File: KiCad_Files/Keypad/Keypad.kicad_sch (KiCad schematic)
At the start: 0 parts

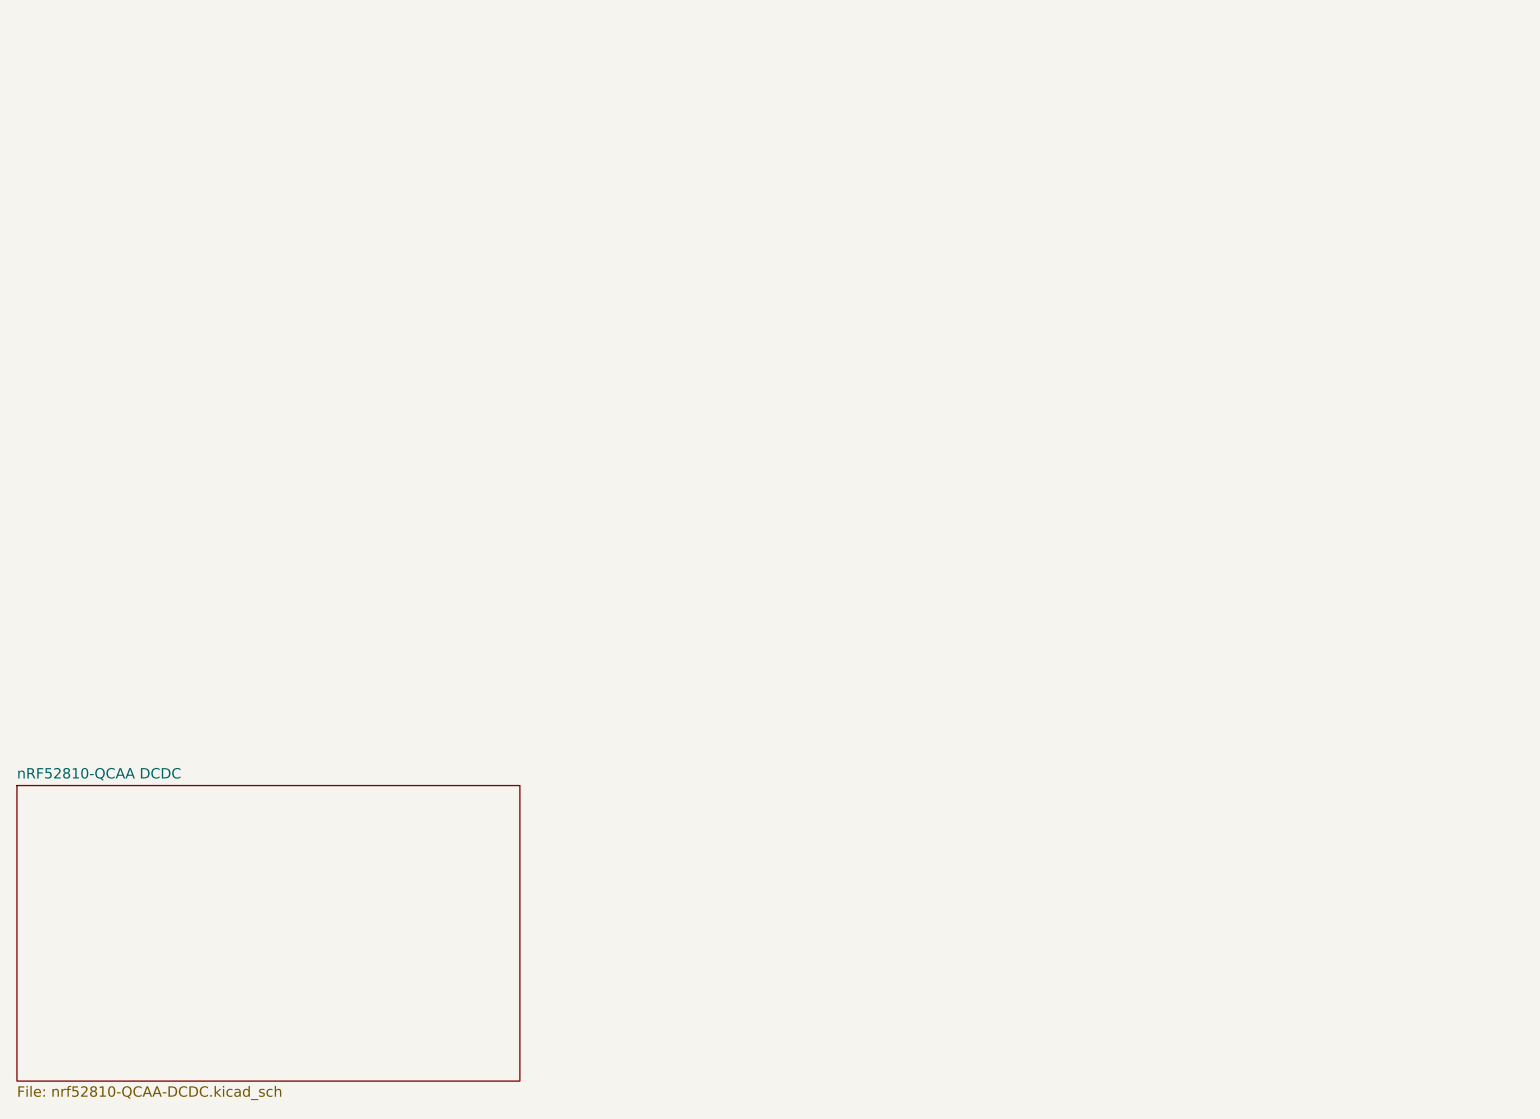
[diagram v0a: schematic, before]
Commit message: Added switch matrix, rotary encoder, slider schematic
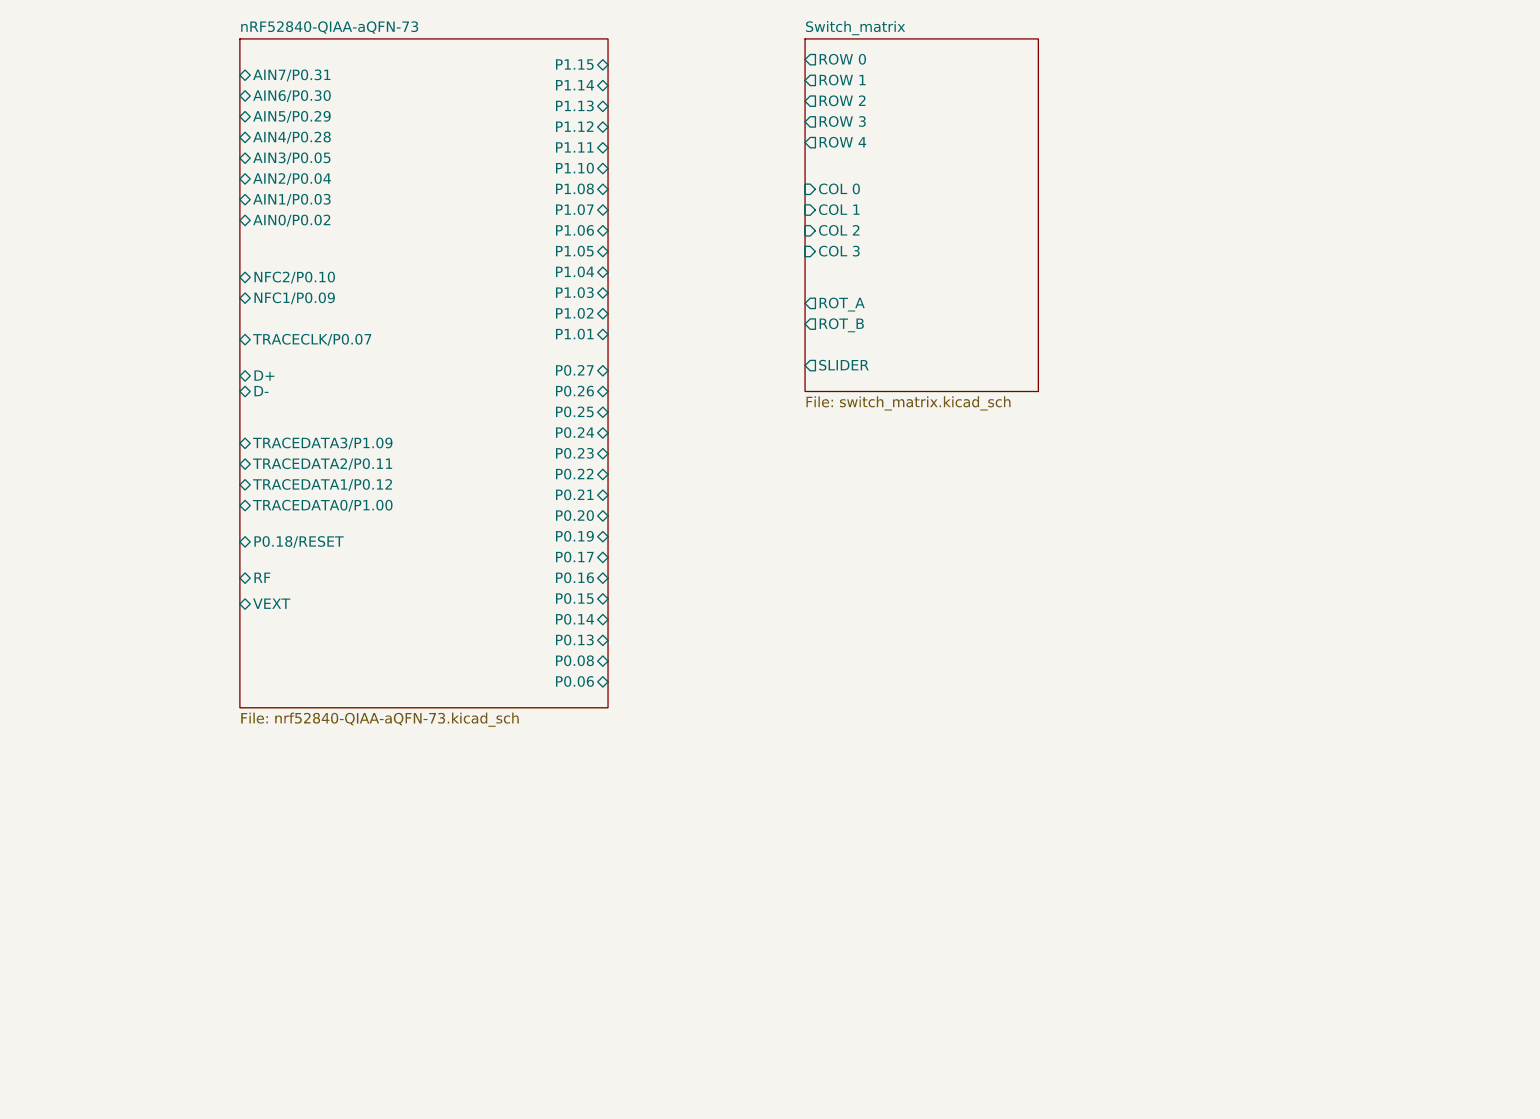
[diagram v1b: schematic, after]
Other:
- removed sheet nRF52810-QCAA DCDC
- added sheet Switch_matrix (switch_matrix.kicad_sch)
- added sheet nRF52840-QIAA-aQFN-73 (nrf52840-QIAA-aQFN-73.kicad_sch)

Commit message: Added schematic for USB C, per key rgb led, 2 types of jtag connectors, rf connector, rotary encoder, slider, and OLED pins
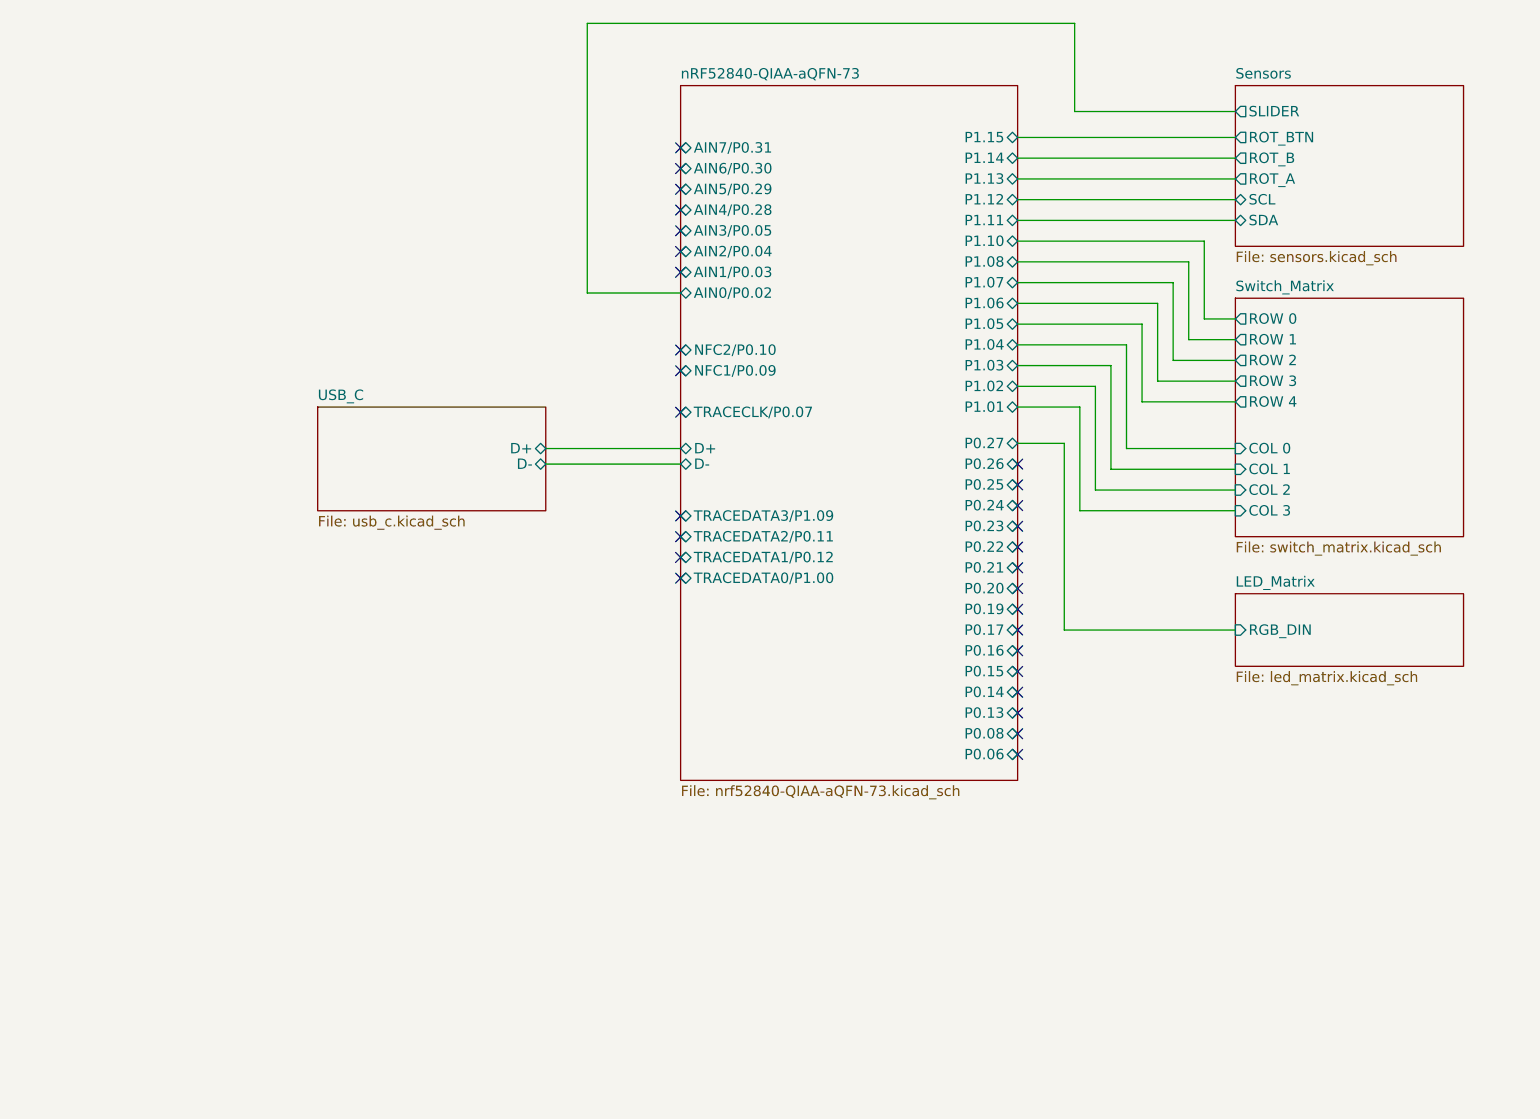
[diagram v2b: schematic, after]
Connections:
- no-connect marks 0 -> 29
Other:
- sheet Switch_matrix renamed Switch_Matrix
- added sheet LED_Matrix (led_matrix.kicad_sch)
- added sheet Sensors (sensors.kicad_sch)
- added sheet USB_C (usb_c.kicad_sch)
- sheet Switch_Matrix ports: added none; removed ROT_A, ROT_B, SLIDER
- sheet nRF52840-QIAA-aQFN-73 ports: added none; removed P0.18/RESET, RF, VEXT
